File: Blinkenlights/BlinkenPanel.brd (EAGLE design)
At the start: 34.3 x 49.2 mm, 33 parts, among them IC3 MCP23017SS

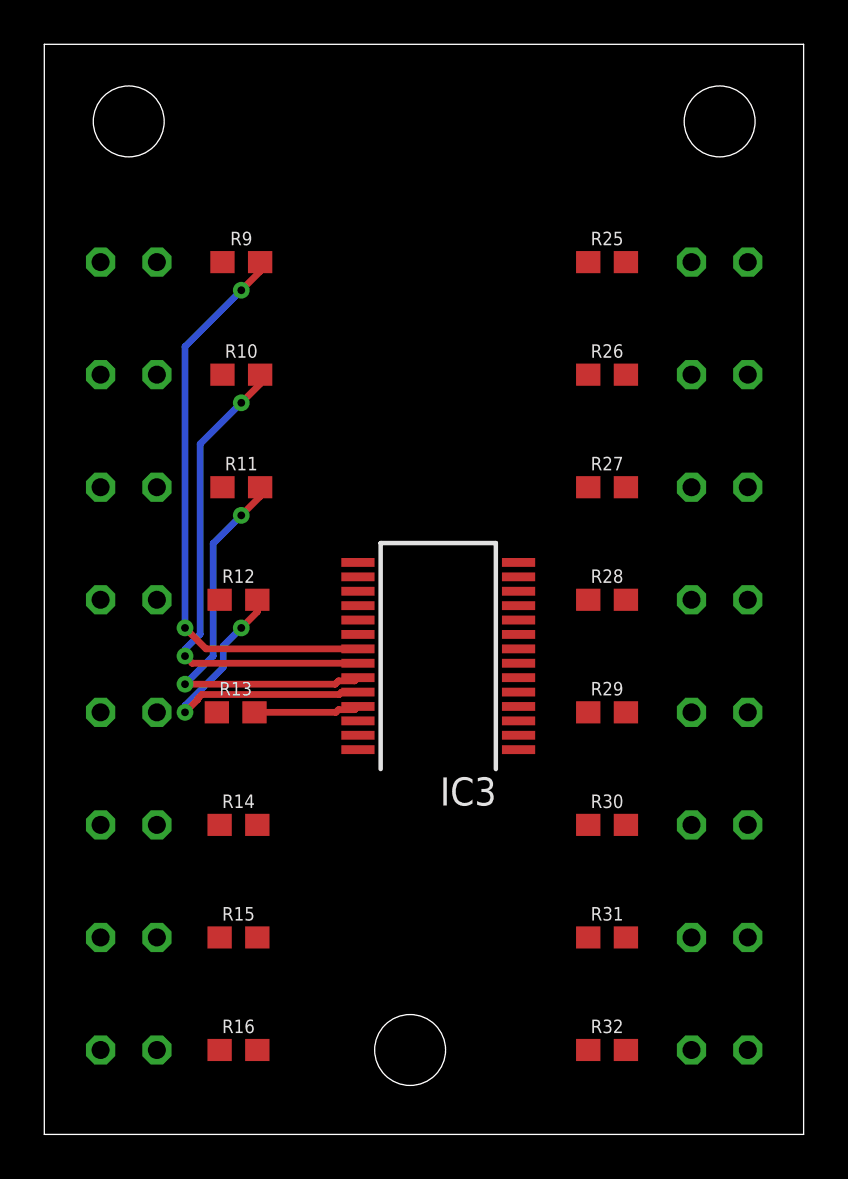
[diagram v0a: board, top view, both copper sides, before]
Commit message: added prints, fixed blinkenpanel
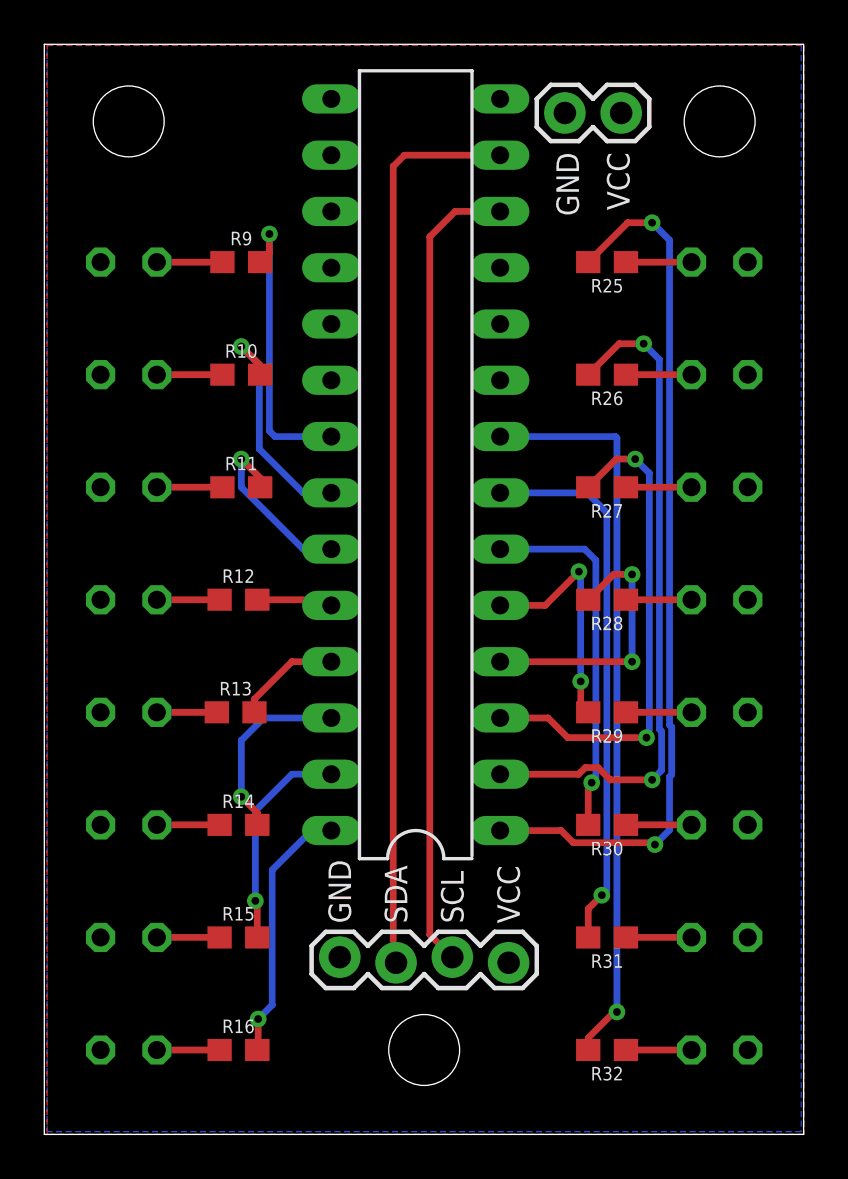
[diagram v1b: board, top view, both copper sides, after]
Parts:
- removed IC3: MCP23017SS, microchip:SSOP28
- added IC1: MCP23017SP, microchip:DIL28-3
- added J1: (no value), SparkFun-Connectors:1X04_LOCK
- added J2: (no value), SparkFun-Connectors:1X02
- turned LED10 to 0 degrees
- turned LED11 to 0 degrees
- turned LED12 to 0 degrees
- turned LED13 to 0 degrees
- turned LED14 to 0 degrees
- turned LED15 to 0 degrees
- turned LED16 to 0 degrees
- turned LED25 to 180 degrees
- turned LED26 to 180 degrees
- turned LED27 to 180 degrees
- turned LED28 to 180 degrees
- turned LED29 to 180 degrees
- turned LED30 to 180 degrees
- turned LED31 to 180 degrees
- turned LED32 to 180 degrees
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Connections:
- removed net VDD: IC3.9
- removed net VSS: IC3.10
- new net GND: IC1.10, IC1.15, IC1.16, IC1.17, J1.1, J2.1, LED10.K, LED11.K, LED12.K, LED13.K, LED14.K, LED15.K, LED16.K, LED25.K, LED26.K, LED27.K, LED28.K, LED29.K, LED30.K, LED31.K, LED32.K, LED9.K
- new net SCL: IC1.12, J1.3
- new net SDA: IC1.13, J1.2
- new net VCC: IC1.18, IC1.9, J1.4, J2.2
- net N$25: now also IC1.21; no longer IC3.21
- net N$26: now also IC1.22; no longer IC3.22
- net N$27: now also IC1.23; no longer IC3.23
- net N$28: now also IC1.24; no longer IC3.24
- net N$29: now also IC1.25; no longer IC3.25
- net N$30: now also IC1.26; no longer IC3.26
- net N$31: now also IC1.27; no longer IC3.27
- net N$32: now also IC1.28; no longer IC3.28
- net N$57: now also IC1.1; no longer IC3.1
- net N$58: now also IC1.2; no longer IC3.2
- net N$59: now also IC1.3; no longer IC3.3
- net N$60: now also IC1.4; no longer IC3.4
- net N$61: now also IC1.5; no longer IC3.5
- net N$62: now also IC1.6; no longer IC3.6
- net N$63: now also IC1.7; no longer IC3.7
- net N$64: now also IC1.8; no longer IC3.8
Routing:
- net SDA: track 0.00 -> 41.0 mm
- net N$57: track 0.00 -> 39.6 mm, vias 0 -> 2
- net SCL: track 0.00 -> 36.6 mm
- net N$64: track 0.00 -> 33.6 mm, vias 0 -> 1
- net N$58: track 0.00 -> 30.5 mm, vias 0 -> 2
- net N$63: track 0.00 -> 24.7 mm, vias 0 -> 1
- net N$59: track 0.00 -> 22.5 mm, vias 0 -> 2
- net N$62: track 0.00 -> 16.6 mm, vias 0 -> 1
- net N$25: track 26.1 -> 13.2 mm, vias 2 -> 1
- net N$60: track 0.00 -> 12.3 mm, vias 0 -> 2
- net N$32: track 0.00 -> 11.8 mm, vias 0 -> 1
- net N$26: track 22.0 -> 10.7 mm, vias 2 -> 1
- net N$28: track 14.6 -> 3.45 mm, vias 2 -> 0
- net N$61: track 0.00 -> 10.7 mm, vias 0 -> 2
- net N$27: track 18.2 -> 8.11 mm, vias 2 -> 1
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- added copper zone on layer 16, net GND
- added copper zone on layer 1, net VCC
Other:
- board text added: "GND"
- board text added: "SCL"
- board text added: "SDA"
- board text added: "VCC"
